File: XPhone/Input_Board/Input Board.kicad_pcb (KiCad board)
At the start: 2 copper layers, 100 x 100 mm, 94 parts, among them J1 AUDIO, J10 ENV, J11 PULSE, J12 PULSE, J13 Power In, J14 Power Out, J2 AUDIO, J3 ENV, J4 ENV, J5 PULSE, J6 PULSE, J7 AUDIO, J8 AUDIO, J9 ENV, Q1 BC847CW, Q2 BC847CW, Q3 BC847CW, Q4 BC847CW, Q5 BC847CW, Q6 BC847CW, Q7 BC847CW, Q8 BC847CW, U1 LM833, U2 78L05, U3 TL084, U4 74HC14, U5 LM833

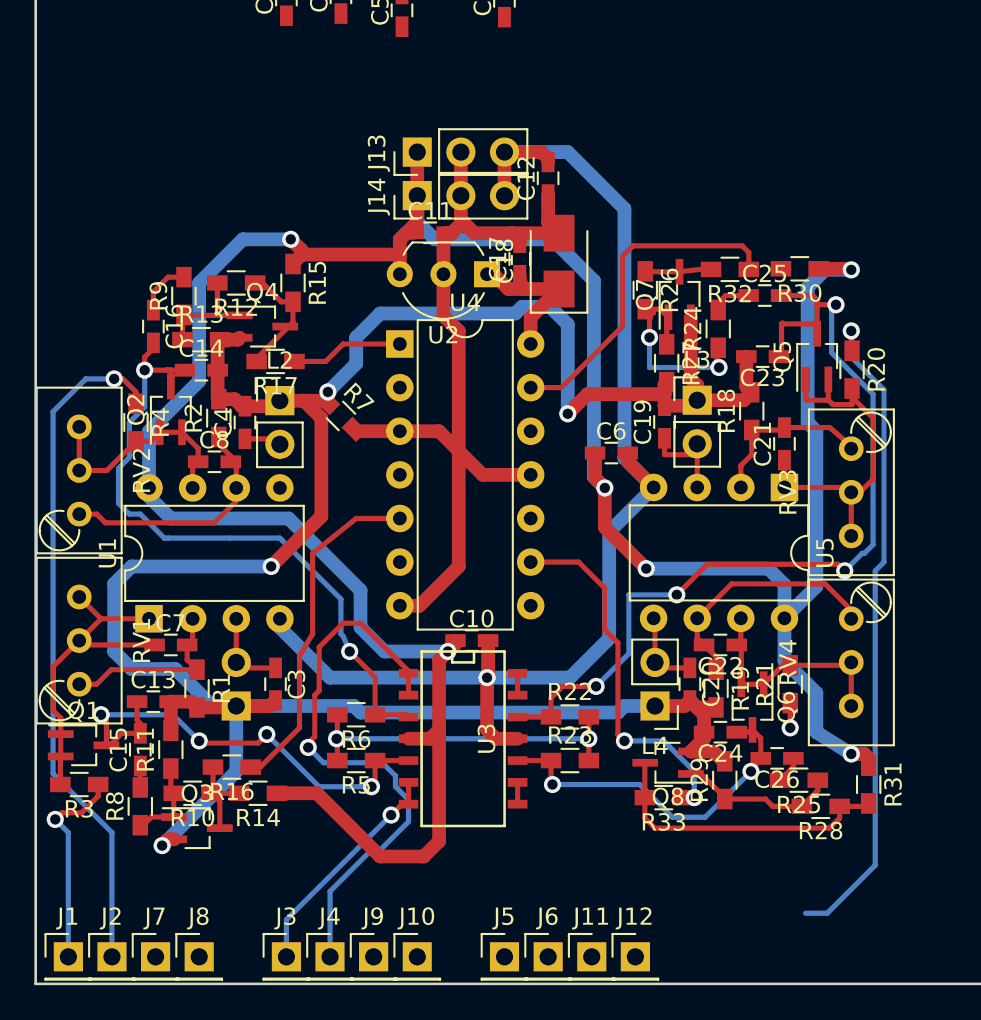
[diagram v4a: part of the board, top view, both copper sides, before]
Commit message: XPhone/Input_Board finished laying out everything of importance (except the V_ENV_BIAS\!
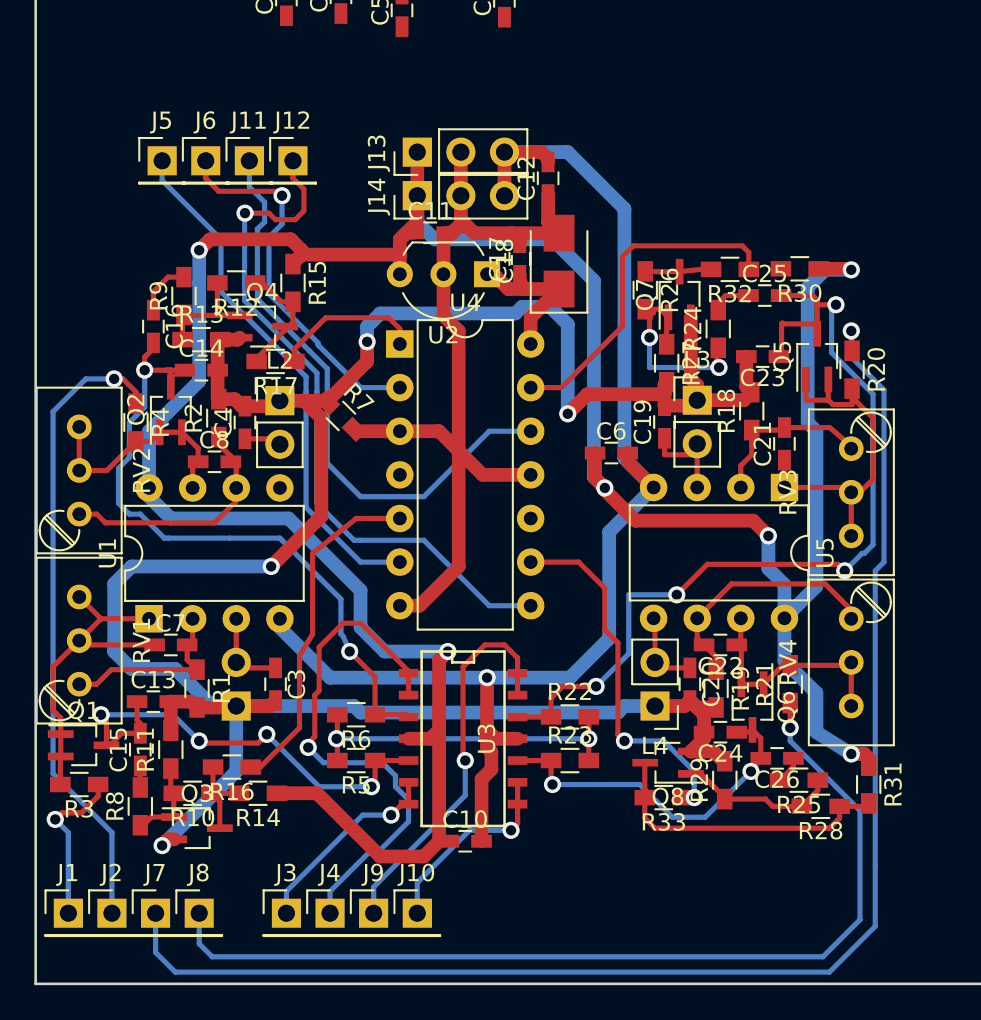
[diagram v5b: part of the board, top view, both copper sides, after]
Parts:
- moved J11 50.5 mm to (12.4, 52.1)
- moved J12 50.5 mm to (15.0, 52.1)
- moved J5 50.5 mm to (7.37, 52.1)
- moved J6 50.5 mm to (9.91, 52.1)
- moved C10 11.7 mm to (25.0, 91.7)
- moved J1 2.54 mm to (1.91, 95.9)
- moved J10 2.54 mm to (22.2, 95.9)
- moved J2 2.54 mm to (4.45, 95.9)
- moved J3 2.54 mm to (14.6, 95.9)
- moved J4 2.54 mm to (17.1, 95.9)
- moved J7 2.54 mm to (6.99, 95.9)
- moved J8 2.54 mm to (9.53, 95.9)
- moved J9 2.54 mm to (19.7, 95.9)
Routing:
- net Net-(J8-Pad1): track 1.44 -> 55.8 mm
- net Net-(J7-Pad1): track 38.5 -> 82.6 mm
- net Net-(J12-Pad1): track 0.00 -> 40.5 mm, vias 0 -> 1
- net Net-(J11-Pad1): track 0.00 -> 34.1 mm
- net Net-(J5-Pad1): track 0.00 -> 30.4 mm
- net Net-(J6-Pad1): track 0.00 -> 21.9 mm, vias 0 -> 1
- net Net-(J9-Pad1): track 1.27 -> 22.8 mm, vias 0 -> 1
- net Net-(J10-Pad1): track 1.27 -> 11.5 mm, vias 0 -> 1
- net -12V: track 72.3 -> 76.9 mm
- net Net-(J4-Pad1): track 33.3 -> 30.7 mm
- net Net-(J1-Pad1): track 12.1 -> 9.60 mm
- net Net-(J2-Pad1): track 39.8 -> 37.2 mm
- net Net-(R17-Pad1): track 6.56 -> 8.76 mm
- net Net-(J3-Pad1): track 13.3 -> 11.8 mm

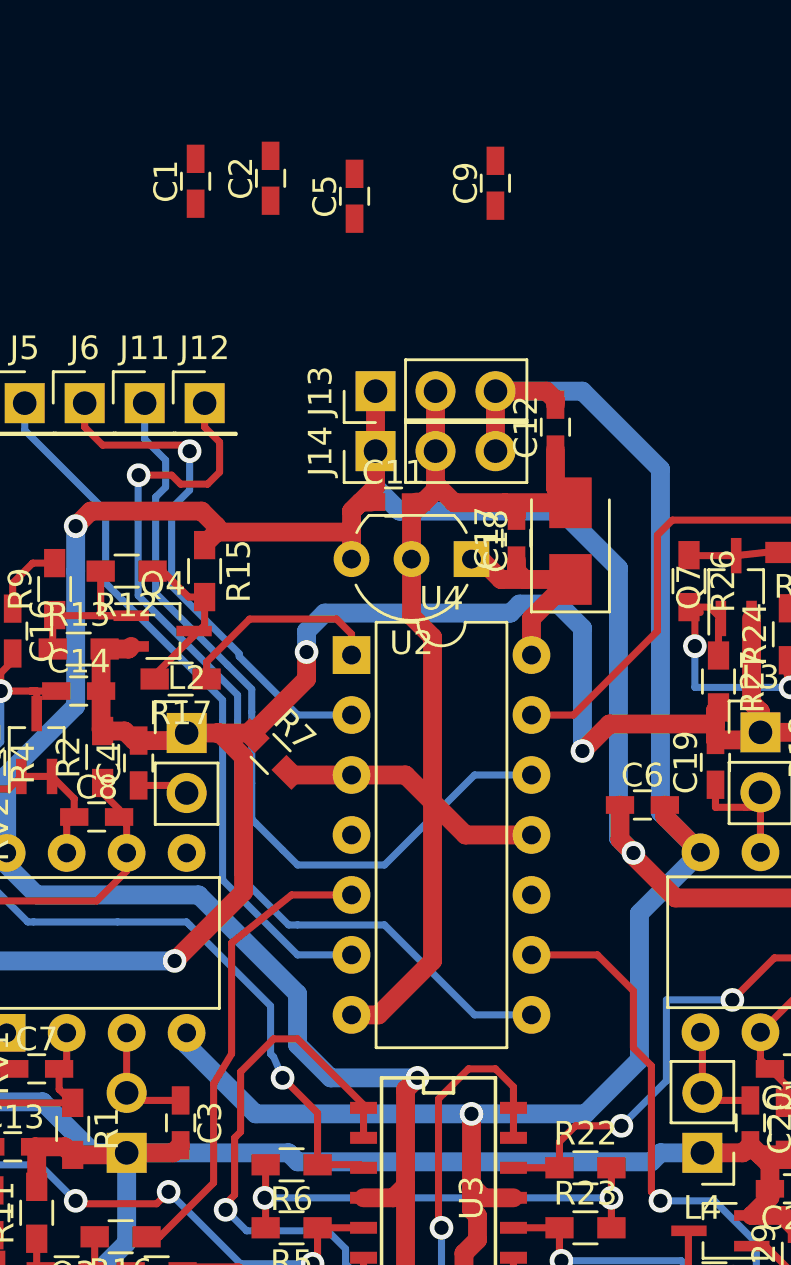
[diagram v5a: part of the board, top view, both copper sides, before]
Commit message: XPhone/Input_Board removing unnecessary caps
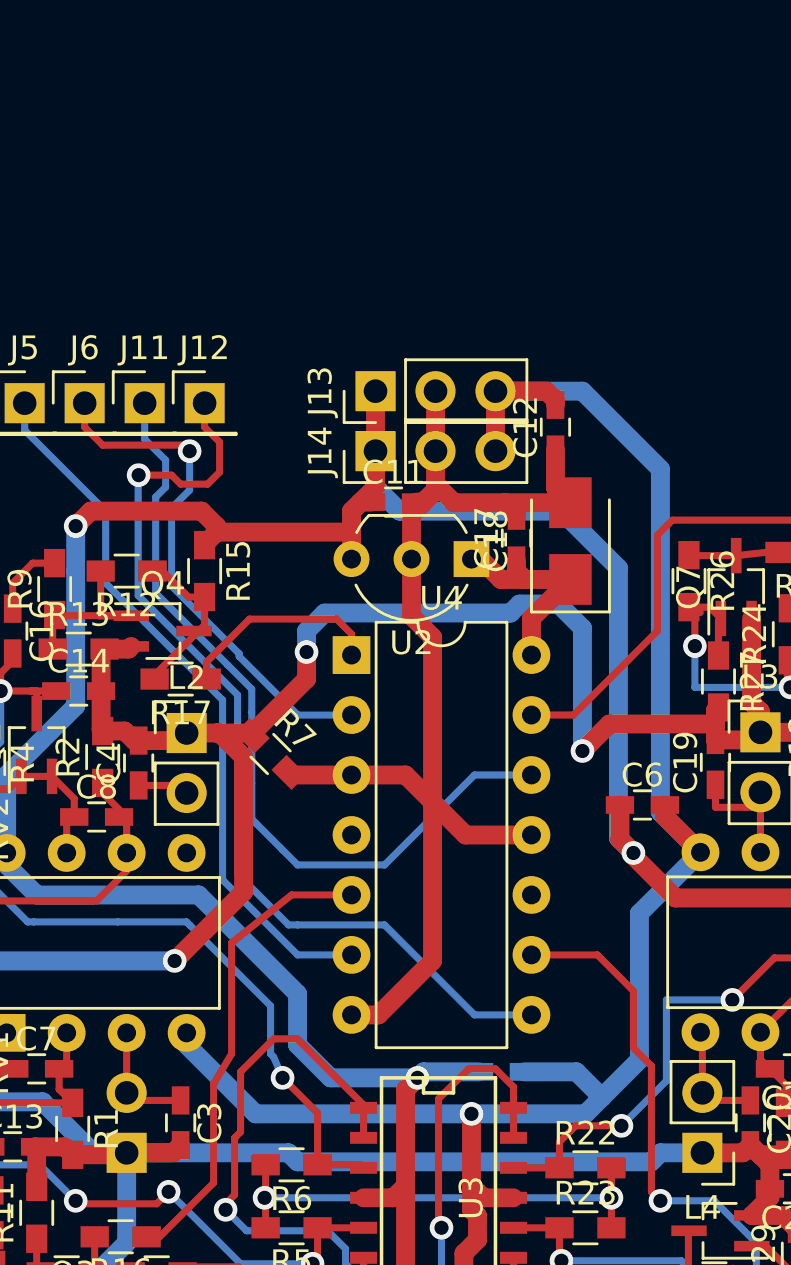
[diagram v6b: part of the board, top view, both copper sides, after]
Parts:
- removed C2, C5, C9: 10n, Capacitors_SMD:C_0603_HandSoldering
- C1: moved to B.Cu
- moved C1 39.9 mm to (27.6, 80.4), turned to 0 degrees
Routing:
- net -12V: track 76.9 -> 80.7 mm
- net +12V: track 164.5 -> 167.3 mm

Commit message: XPhone/Input_Board final commit for the night
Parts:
- moved C25 1.69 mm to (42.3, 61.6)
- moved R19 0.13 mm to (39.6, 82.7)
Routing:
- net Net-(Q7-Pad3): track 4.45 -> 10.2 mm
- net Net-(C4-Pad1): track 2.16 -> 4.70 mm
- net Net-(C23-Pad1): track 53.1 -> 50.6 mm
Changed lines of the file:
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@@
   (general
     (links 169)
-    (no_connects 2)
-    (area -0.075001 -0.075001 100.075001 100.075001)
+    (no_connects 0)
+    (area -1.206 -0.100001 100.100001 100.100001)
     (thickness 1.6)
     (drawings 6)
-    (tracks 680)
+    (tracks 684)
     (zones 0)
     (modules 91)
@@
     (visible_elements 7FFCFFFF)
     (pcbplotparams
-      (layerselection 0x20000_00000001)
+      (layerselection 0x310f0_80000001)
       (usegerberextensions false)
       (excludeedgelayer true)
@@
       (padsonsilk false)
       (subtractmaskfromsilk false)
-      (outputformat 4)
+      (outputformat 1)
       (mirror false)
       (drillshape 0)
@@
   )
   (module Capacitors_SMD:C_0603_HandSoldering (layer F.Cu)
-    (at 42.464 59.916)
+    (at 42.291 61.595)
     (descr "Capacitor SMD 0603, hand soldering")
     (tags "capacitor 0603")
@@
   )
   (module Resistors_SMD:R_0603_HandSoldering (layer F.Cu)
-    (at 39.624 82.804 270)
+    (at 39.624 82.677 270)
     (descr "Resistor SMD 0603, hand soldering")
     (tags "resistor 0603")
@@
   (segment (start 38.928 85.344) (end 38.928 84.328) (width 0.8) (layer F.Cu) (net 3))
   (segment (start 38.928 84.328) (end 38.1 83.5) (width 0.8) (layer F.Cu) (net 3))
-  (segment (start 39.624 83.904) (end 38.504 83.904) (width 0.8) (layer F.Cu) (net 3))
+  (segment (start 39.624 83.777) (end 38.504 83.904) (width 0.8) (layer F.Cu) (net 3) (status 10))
   (segment (start 38.504 83.904) (end 38.1 83.5) (width 0.8) (layer F.Cu) (net 3))
   (segment (start 36.622 66.332) (end 36.622 65.659) (width 0.8) (layer F.Cu) (net 3))
@@
   (segment (start 41.237 66.012) (end 41.702 65.547) (width 0.8) (layer F.Cu) (net 3))
   (segment (start 41.387 63.472) (end 41.387 65.232) (width 0.8) (layer F.Cu) (net 3))
+  (segment (start 14.224 68.58) (end 14.224 71.12) (width 0.3) (layer F.Cu) (net 4))
   (segment (start 12.192 68.26) (end 13.904 68.26) (width 0.3) (layer F.Cu) (net 4))
   (segment (start 13.904 68.26) (end 14.224 68.58) (width 0.3) (layer F.Cu) (net 4))
@@
   (segment (start 38.527 78.712) (end 38.527 79.863) (width 0.3) (layer F.Cu) (net 20))
   (segment (start 38.527 79.863) (end 38.928 80.264) (width 0.3) (layer F.Cu) (net 20))
-  (segment (start 39.624 81.704) (end 39.624 80.96) (width 0.3) (layer F.Cu) (net 20))
+  (segment (start 39.624 81.577) (end 39.624 80.96) (width 0.3) (layer F.Cu) (net 20) (status 10))
   (segment (start 39.624 80.96) (end 38.928 80.264) (width 0.3) (layer F.Cu) (net 20))
   (segment (start 30.015 84.455) (end 30.015 83.355) (width 0.3) (layer F.Cu) (net 21))
@@
   (segment (start 30.015 84.455) (end 28.067 84.455) (width 0.3) (layer F.Cu) (net 21))
   (segment (start 43.287 63.472) (end 43.287 63.607) (width 0.3) (layer F.Cu) (net 21))
-  (segment (start 43.414 59.916) (end 45.258 59.916) (width 0.3) (layer F.Cu) (net 21))
-  (segment (start 45.258 59.916) (end 45.512 60.17) (width 0.3) (layer F.Cu) (net 21))
-  (segment (start 45.512 60.17) (end 45.512 60.452) (width 0.3) (layer F.Cu) (net 21))
   (segment (start 45.512 60.452) (end 45.512 62.142) (width 0.3) (layer F.Cu) (net 21))
   (segment (start 43.437 61.567) (end 45.512 61.567) (width 0.3) (layer F.Cu) (net 21))
@@
   (segment (start 40.828 85.344) (end 41.614 85.344) (width 0.3) (layer F.Cu) (net 22))
   (segment (start 41.614 85.344) (end 41.746 84.958) (width 0.3) (layer F.Cu) (net 22))
-  (segment (start 41.514 59.916) (end 40.178 59.916) (width 0.3) (layer F.Cu) (net 23))
+  (segment (start 39.75 60.758) (end 40.842 60.758) (width 0.3) (layer F.Cu) (net 23))
+  (segment (start 40.842 60.758) (end 41.341 61.257) (width 0.3) (layer F.Cu) (net 23))
+  (segment (start 41.341 61.257) (end 41.341 61.595) (width 0.3) (layer F.Cu) (net 23))
   (segment (start 39.797 60.297) (end 39.5 60.758) (width 0.3) (layer F.Cu) (net 23) (status 30))
-  (segment (start 40.178 59.916) (end 39.797 60.297) (width 0.3) (layer F.Cu) (net 23) (status 20))
-  (segment (start 41.514 59.916) (end 41.514 60.17) (width 0.3) (layer F.Cu) (net 23))
+  (segment (start 41.341 61.595) (end 41.341 61.849) (width 0.3) (layer F.Cu) (net 23) (status 30))
   (segment (start 44.13 86.868) (end 44.13 87.358) (width 0.3) (layer F.Cu) (net 24))
   (segment (start 44.13 87.358) (end 43.35 88.138) (width 0.3) (layer F.Cu) (net 24))
@@
   (segment (start 38.75 87.772) (end 40.132 89.154) (width 0.3) (layer F.Cu) (net 45))
   (segment (start 40.132 89.154) (end 40.132 89.238) (width 0.3) (layer F.Cu) (net 45))
+  (segment (start 43.4 58.358) (end 43.4 59.089) (width 0.3) (layer F.Cu) (net 46))
+  (segment (start 39.332 58.89) (end 39.332 58.392) (width 0.3) (layer F.Cu) (net 46))
+  (segment (start 40.005 59.563) (end 39.332 58.89) (width 0.3) (layer F.Cu) (net 46))
+  (segment (start 42.926 59.563) (end 40.005 59.563) (width 0.3) (layer F.Cu) (net 46))
+  (segment (start 43.4 59.089) (end 42.926 59.563) (width 0.3) (layer F.Cu) (net 46))
   (segment (start 37.5 58.528) (end 35.52 58.528) (width 0.3) (layer F.Cu) (net 46))
   (segment (start 35.52 58.528) (end 35.5 58.508) (width 0.3) (layer F.Cu) (net 46))

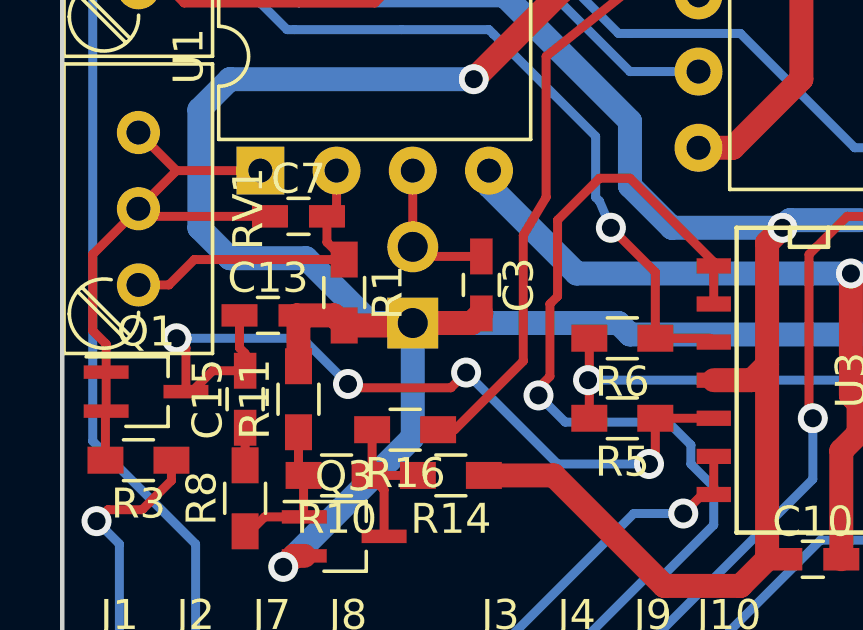
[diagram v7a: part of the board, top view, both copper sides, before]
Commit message: XPhone/Input_Board fixed L orientation (not a big deal, but it bugged me)
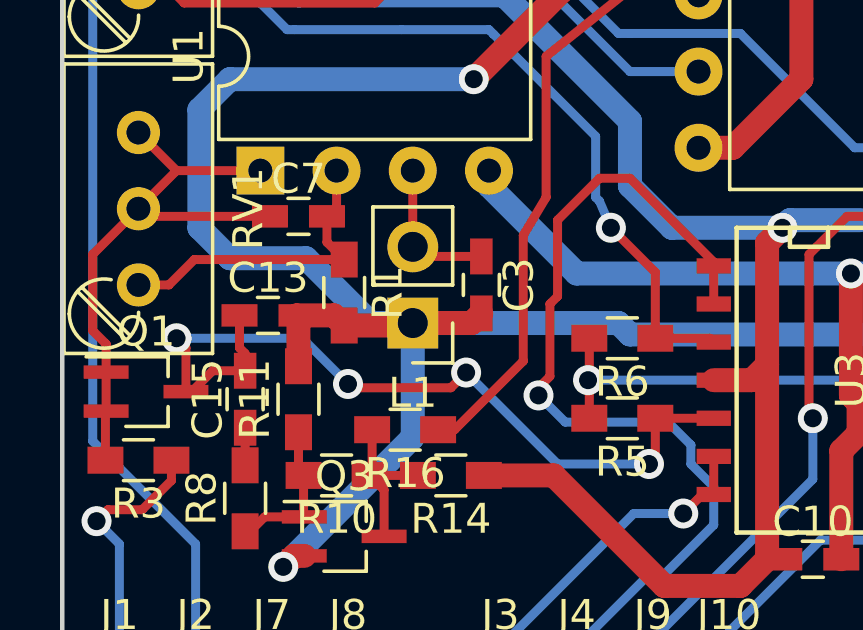
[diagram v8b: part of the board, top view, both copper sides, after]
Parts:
- L1: moved to F.Cu
- turned L1 to 180 degrees
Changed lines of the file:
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@@
     (links 169)
     (no_connects 0)
-    (area -1.206 -0.100001 100.100001 100.100001)
+    (area -0.075001 -0.075001 100.075001 100.075001)
     (thickness 1.6)
     (drawings 6)
@@
     )
   )
-  (module Pin_Headers:Pin_Header_Straight_1x02_Pitch2.54mm (layer B.Cu)
-    (at 11.684 83.82)
+  (module Pin_Headers:Pin_Header_Straight_1x02_Pitch2.54mm (layer F.Cu)
+    (at 11.684 83.82 180)
     (descr "Through hole straight pin header, 1x02, 2.54mm pitch, single row")
     (tags "Through hole pin header THT 1x02 2.54mm single row")
-    (fp_text reference L1 (at 0 2.33) (layer B.SilkS)
-      (effects (font (size 1 1) (thickness 0.15)) (justify mirror))
-    )
-    (fp_text value "Input Coil" (at 0 -4.87) (layer B.Fab)
-      (effects (font (size 1 1) (thickness 0.15)) (justify mirror))
-    )
-    (fp_line (start -1.27 1.27) (end -1.27 -3.81) (layer B.Fab) (width 0.1))
-    (fp_line (start -1.27 -3.81) (end 1.27 -3.81) (layer B.Fab) (width 0.1))
-    (fp_line (start 1.27 -3.81) (end 1.27 1.27) (layer B.Fab) (width 0.1))
-    (fp_line (start 1.27 1.27) (end -1.27 1.27) (layer B.Fab) (width 0.1))
-    (fp_line (start -1.33 -1.27) (end -1.33 -3.87) (layer B.SilkS) (width 0.12))
-    (fp_line (start -1.33 -3.87) (end 1.33 -3.87) (layer B.SilkS) (width 0.12))
-    (fp_line (start 1.33 -3.87) (end 1.33 -1.27) (layer B.SilkS) (width 0.12))
-    (fp_line (start 1.33 -1.27) (end -1.33 -1.27) (layer B.SilkS) (width 0.12))
-    (fp_line (start -1.33 0) (end -1.33 1.33) (layer B.SilkS) (width 0.12))
-    (fp_line (start -1.33 1.33) (end 0 1.33) (layer B.SilkS) (width 0.12))
-    (fp_line (start -1.8 1.8) (end -1.8 -4.35) (layer B.CrtYd) (width 0.05))
-    (fp_line (start -1.8 -4.35) (end 1.8 -4.35) (layer B.CrtYd) (width 0.05))
-    (fp_line (start 1.8 -4.35) (end 1.8 1.8) (layer B.CrtYd) (width 0.05))
-    (fp_line (start 1.8 1.8) (end -1.8 1.8) (layer B.CrtYd) (width 0.05))
-    (fp_text user %R (at 0 2.33) (layer B.Fab)
-      (effects (font (size 1 1) (thickness 0.15)) (justify mirror))
-    )
-    (pad 1 thru_hole rect (at 0 0) (size 1.7 1.7) (drill 1) (layers *.Cu *.Mask)
+    (fp_text reference L1 (at 0 -2.33 180) (layer F.SilkS)
+      (effects (font (size 1 1) (thickness 0.15)))
+    )
+    (fp_text value "Input Coil" (at 0 4.87 180) (layer F.Fab)
+      (effects (font (size 1 1) (thickness 0.15)))
+    )
+    (fp_line (start -1.27 -1.27) (end -1.27 3.81) (layer F.Fab) (width 0.1))
+    (fp_line (start -1.27 3.81) (end 1.27 3.81) (layer F.Fab) (width 0.1))
+    (fp_line (start 1.27 3.81) (end 1.27 -1.27) (layer F.Fab) (width 0.1))
+    (fp_line (start 1.27 -1.27) (end -1.27 -1.27) (layer F.Fab) (width 0.1))
+    (fp_line (start -1.33 1.27) (end -1.33 3.87) (layer F.SilkS) (width 0.12))
+    (fp_line (start -1.33 3.87) (end 1.33 3.87) (layer F.SilkS) (width 0.12))
+    (fp_line (start 1.33 3.87) (end 1.33 1.27) (layer F.SilkS) (width 0.12))
+    (fp_line (start 1.33 1.27) (end -1.33 1.27) (layer F.SilkS) (width 0.12))
+    (fp_line (start -1.33 0) (end -1.33 -1.33) (layer F.SilkS) (width 0.12))
+    (fp_line (start -1.33 -1.33) (end 0 -1.33) (layer F.SilkS) (width 0.12))
+    (fp_line (start -1.8 -1.8) (end -1.8 4.35) (layer F.CrtYd) (width 0.05))
+    (fp_line (start -1.8 4.35) (end 1.8 4.35) (layer F.CrtYd) (width 0.05))
+    (fp_line (start 1.8 4.35) (end 1.8 -1.8) (layer F.CrtYd) (width 0.05))
+    (fp_line (start 1.8 -1.8) (end -1.8 -1.8) (layer F.CrtYd) (width 0.05))
+    (fp_text user %R (at 0 -2.33 180) (layer F.Fab)
+      (effects (font (size 1 1) (thickness 0.15)))
+    )
+    (pad 1 thru_hole rect (at 0 0 180) (size 1.7 1.7) (drill 1) (layers *.Cu *.Mask)
       (net 3 GNDA))
-    (pad 2 thru_hole oval (at 0 -2.54) (size 1.7 1.7) (drill 1) (layers *.Cu *.Mask)
+    (pad 2 thru_hole oval (at 0 2.54 180) (size 1.7 1.7) (drill 1) (layers *.Cu *.Mask)
       (net 2 "Net-(C3-Pad1)"))
     (model ${KISYS3DMOD}/Pin_Headers.3dshapes/Pin_Header_Straight_1x02_Pitch2.54mm.wrl
